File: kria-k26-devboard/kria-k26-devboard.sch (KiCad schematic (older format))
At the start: 1 part

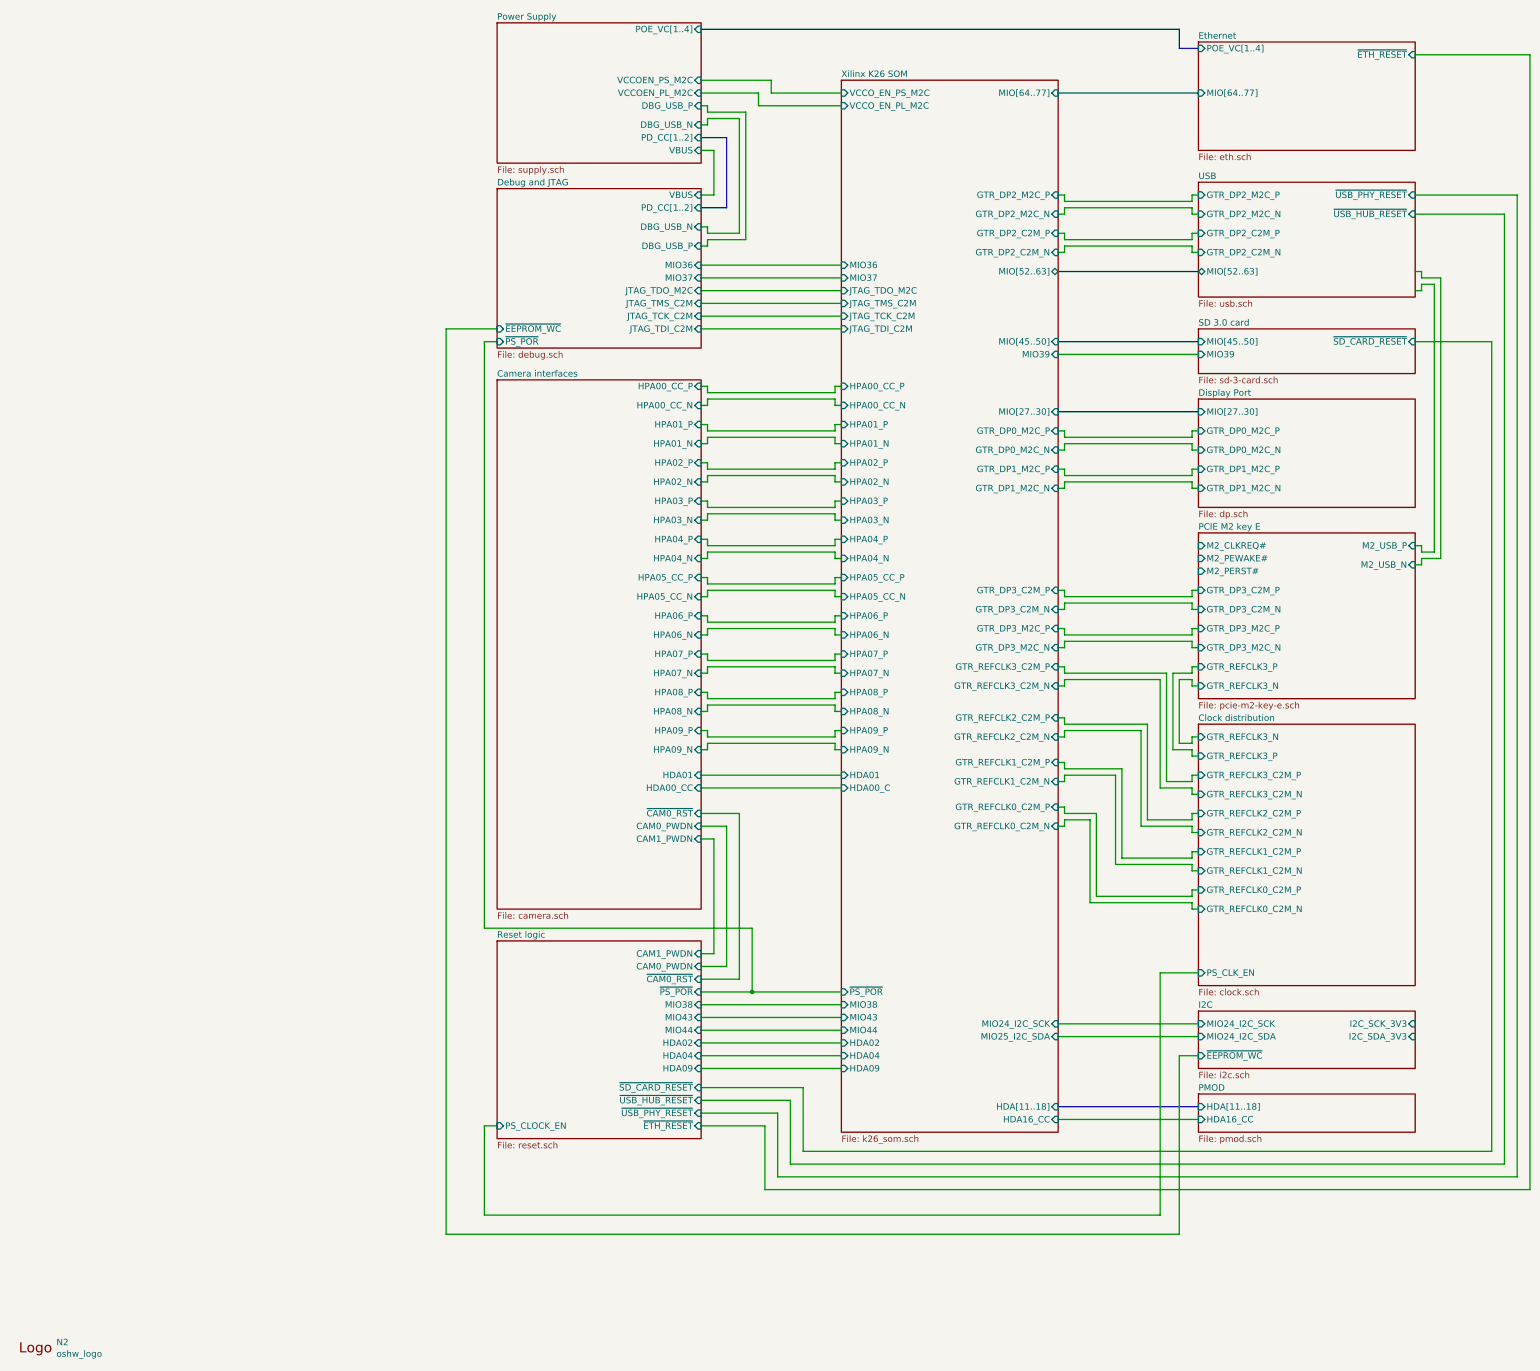
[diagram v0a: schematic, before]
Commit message: Added Led voltage indicator, fan circuit. Tidied up supply and SOM sheet
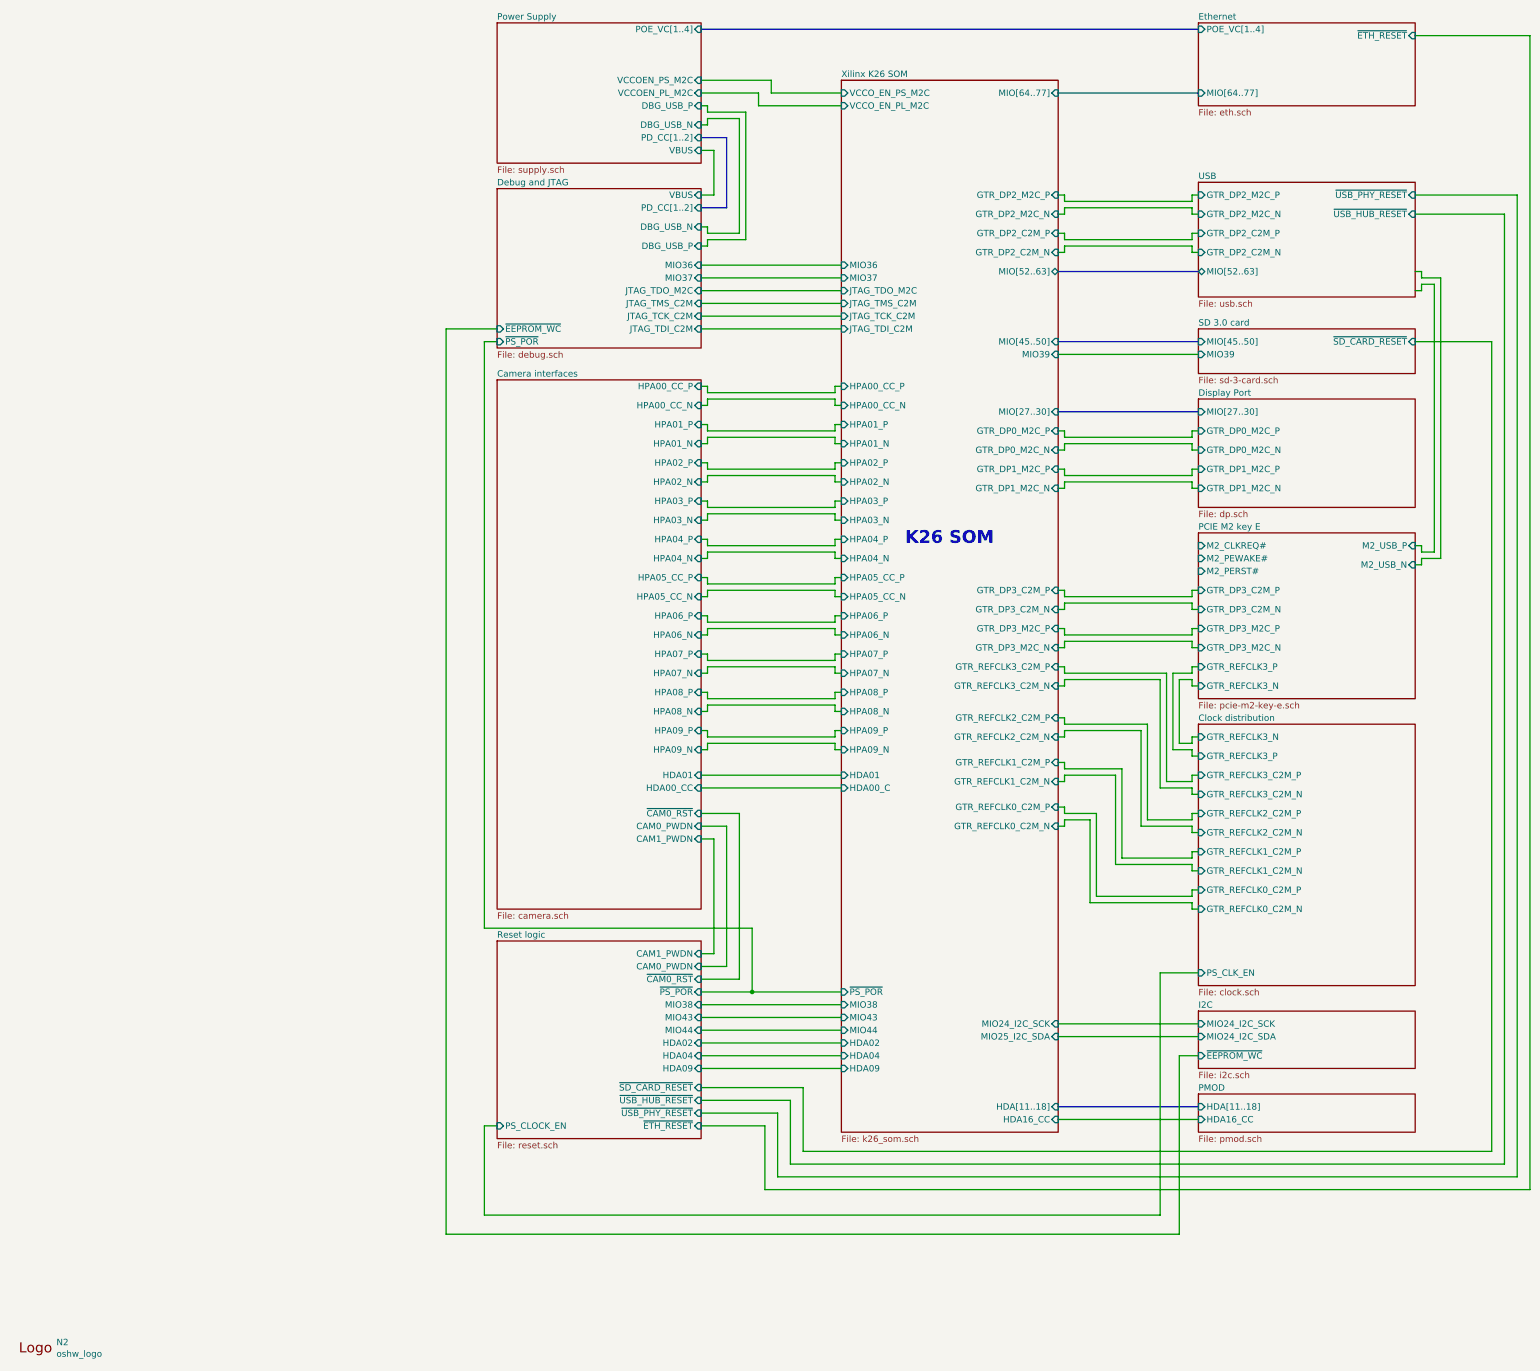
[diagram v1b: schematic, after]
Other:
- note added: "K26 SOM"
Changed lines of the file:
@@
 $EndSheet
-Wire Wire Line
-	12450 9800 12450 900
 Wire Wire Line
 	12150 3150 11550 3150
@@
 	12350 2000 12350 9700
 Wire Wire Line
-	12450 900  11550 900
+	12450 750  11550 750
 Wire Wire Line
 	5950 2250 6000 2250
@@
 F2 "MIO24_I2C_SCK" I L 9850 8500 50
 F3 "MIO24_I2C_SDA" I L 9850 8600 50
-F4 "I2C_SDA_3V3" I R 11550 8600 50
-F5 "I2C_SCK_3V3" I R 11550 8500 50
-F6 "~EEPROM_WC" I L 9850 8750 50
+F4 "~EEPROM_WC" I L 9850 8750 50
 $EndSheet
 Wire Wire Line
@@
 Wire Wire Line
 	6050 1650 5950 1650
-Wire Bus Line
-	5950 700  9700 700
-Wire Bus Line
-	9700 700  9700 850
-Wire Bus Line
-	9700 850  9850 850
 $Sheet
 S 9850 1900 1700 900
@@
 $EndSheet
 $Sheet
-S 9850 800  1700 850
+S 9850 650  1700 650
 U 63C3FA95
 F0 "Ethernet" 50
 F1 "eth.sch" 50
 F2 "MIO[64..77]" I L 9850 1200 50
-F3 "POE_VC[1..4]" I L 9850 850 50
-F4 "~ETH_RESET" I R 11550 900 50
+F3 "POE_VC[1..4]" I L 9850 700 50
+F4 "~ETH_RESET" I R 11550 750 50
 $EndSheet
 $Sheet
@@
 Wire Wire Line
 	9700 8750 9850 8750
+Wire Bus Line
+	5950 700  9850 700
+Wire Wire Line
+	12450 750  12450 9800
+Text Notes 7550 4750 0    100  ~ 20
+K26 SOM
 $EndSCHEMATC

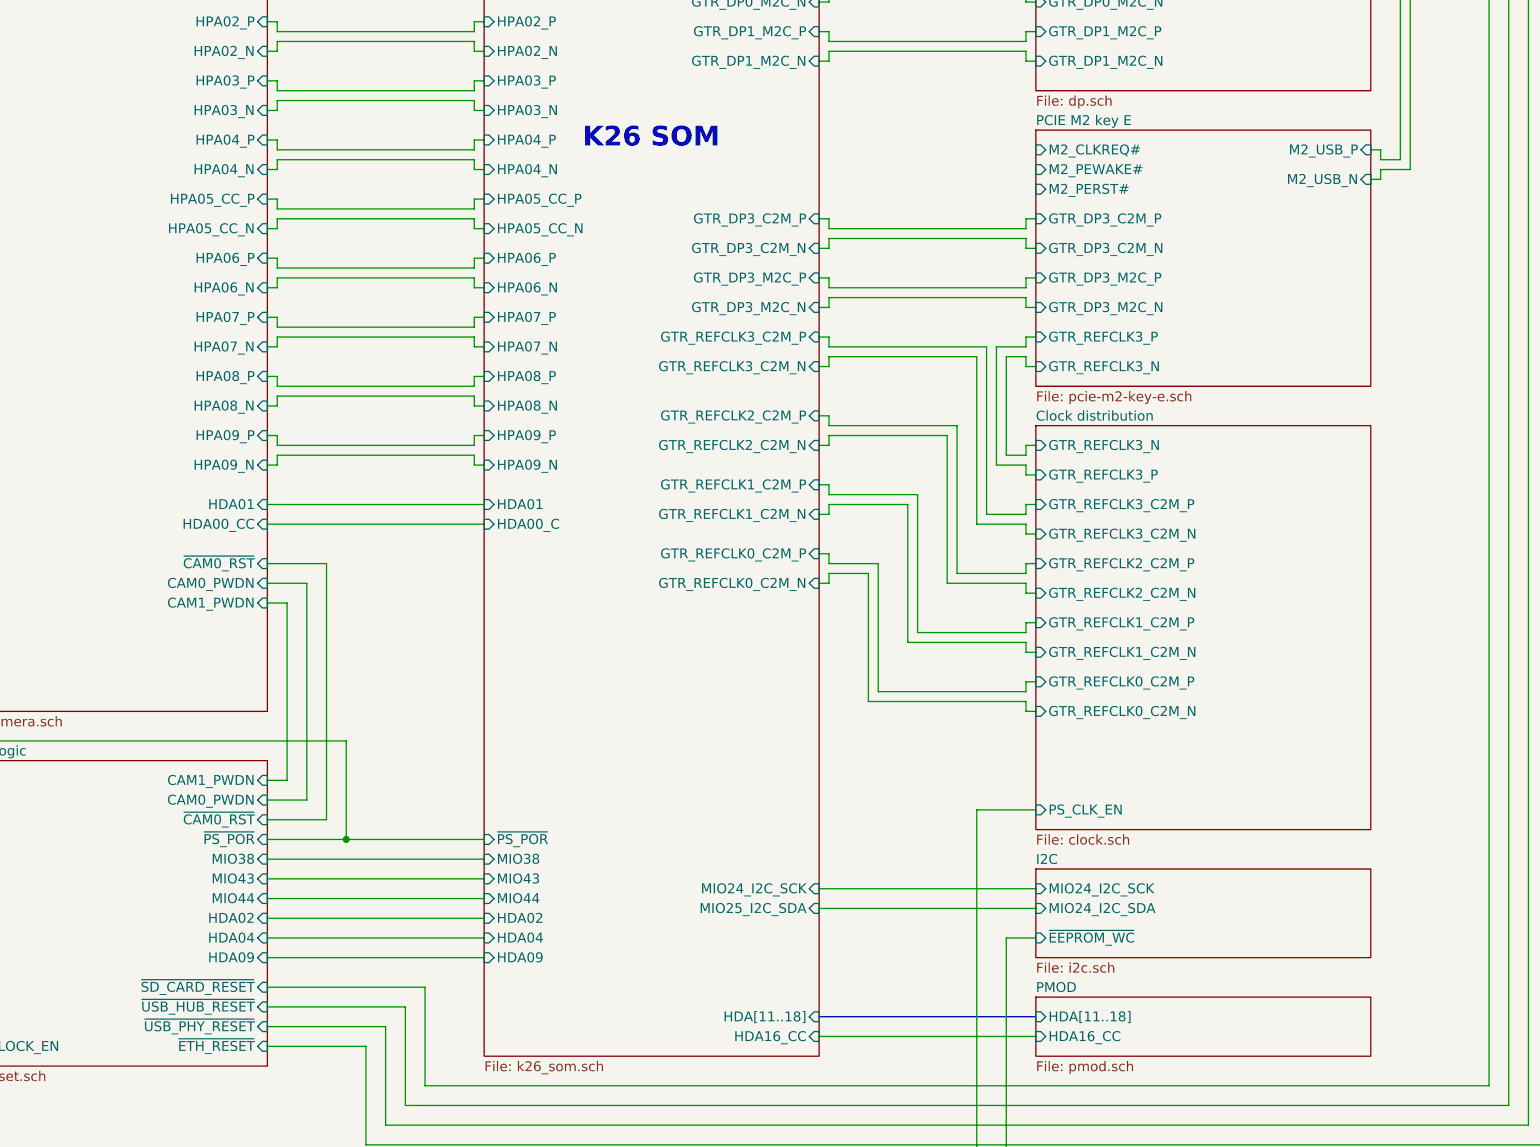
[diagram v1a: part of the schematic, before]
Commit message: fixed an issue with reset logic (Mixed PS and PL domain on OD buffer), extended the logic circuit to support M.2 PERST# (reset for PCIe WIFI), fixed the polarity of the camera control signal CAM_RST to comply with Antmicro standard, change CAM _SHDN to CAM_VSYNC, replaced the reset connector to fit additional signal M2_PERST
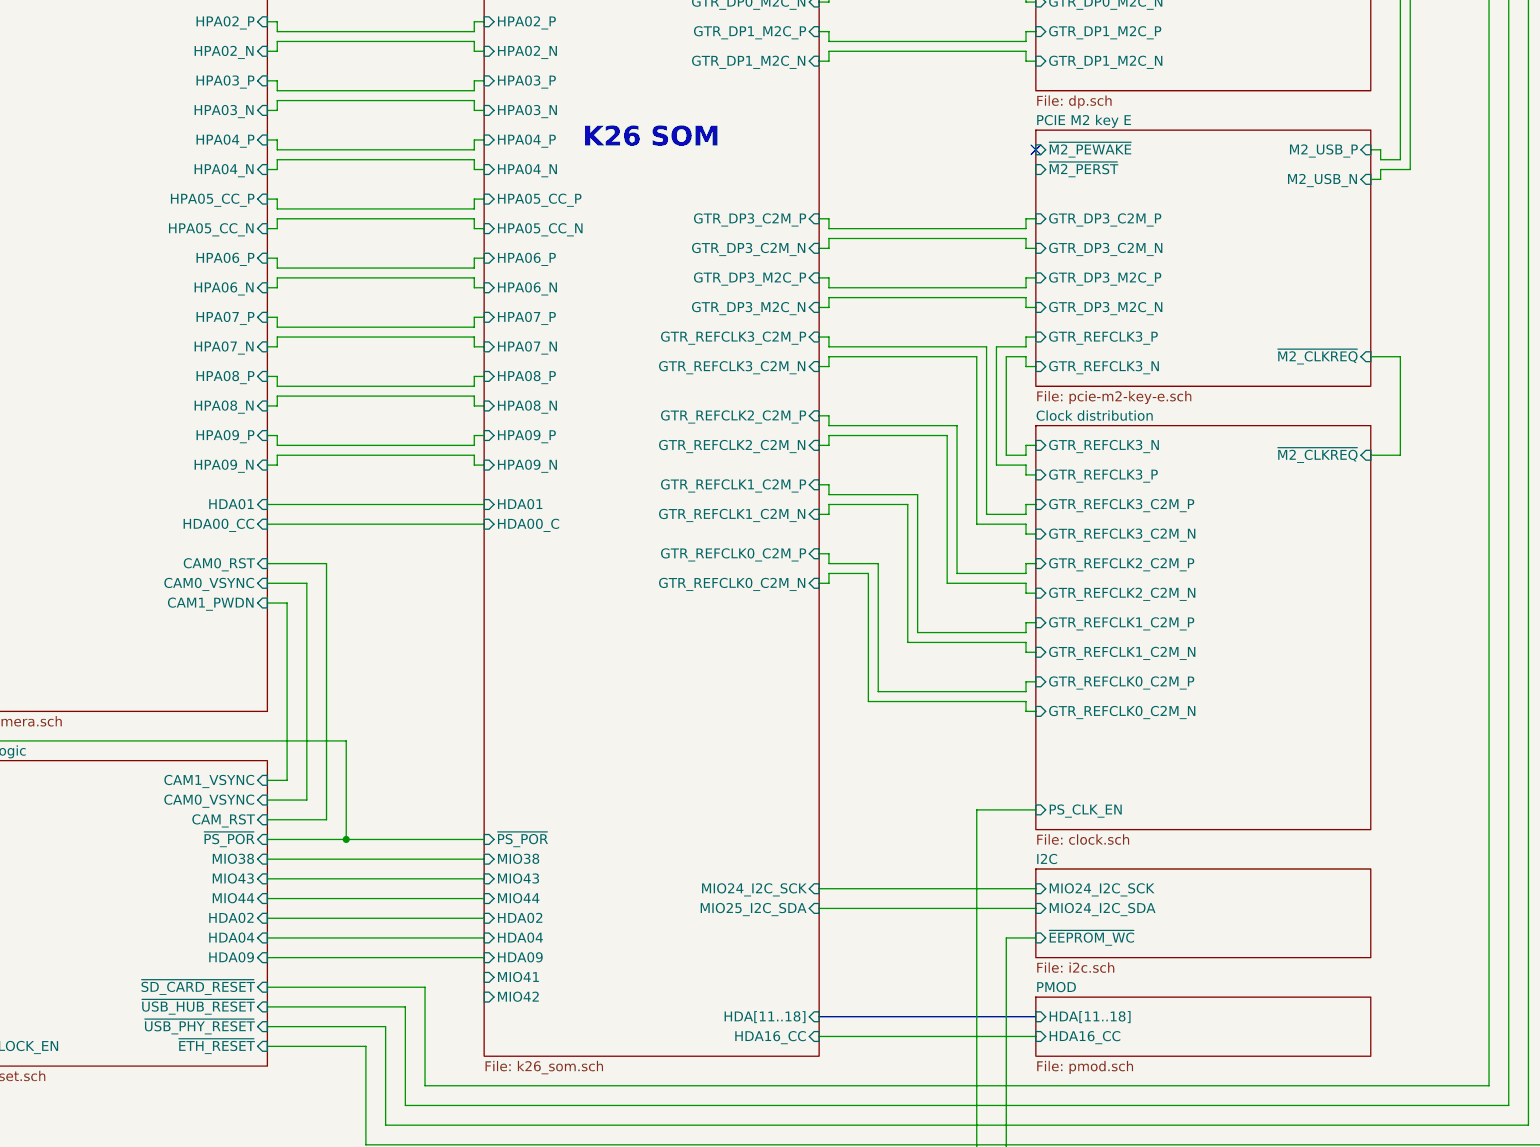
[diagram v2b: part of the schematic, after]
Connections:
- no-connect marks 0 -> 1
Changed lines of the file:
@@
 F6 "GTR_REFCLK3_P" I L 9850 5700 50
 F7 "GTR_REFCLK3_N" I L 9850 5850 50
-F8 "M2_CLKREQ#" I L 9850 4750 50
-F9 "M2_PEWAKE#" I L 9850 4850 50
-F10 "M2_PERST#" I L 9850 4950 50
-F11 "M2_USB_P" I R 11550 4750 50
-F12 "M2_USB_N" I R 11550 4900 50
+F8 "M2_USB_P" I R 11550 4750 50
+F9 "M2_USB_N" I R 11550 4900 50
+F10 "~M2_CLKREQ" I R 11550 5800 50
+F11 "~M2_PEWAKE" I L 9850 4750 50
+F12 "~M2_PERST" I L 9850 4850 50
 $EndSheet
 Wire Wire Line
@@
 F11 "GTR_REFCLK0_C2M_P" I L 9850 7450 50
 F12 "GTR_REFCLK0_C2M_N" I L 9850 7600 50
+F13 "~M2_CLKREQ" I R 11550 6300 50
 $EndSheet
 Wire Wire Line
@@
 F22 "HDA01" I R 5950 6550 50
 F23 "HDA00_CC" I R 5950 6650 50
-F24 "CAM0_PWDN" I R 5950 6950 50
-F25 "CAM1_PWDN" I R 5950 7050 50
-F26 "~CAM0_RST" I R 5950 6850 50
+F24 "CAM0_RST" I R 5950 6850 50
+F25 "CAM0_VSYNC" I R 5950 6950 50
+F26 "CAM1_PWDN" I R 5950 7050 50
 $EndSheet
 Wire Wire Line
@@
 Wire Wire Line
 	7050 8850 5950 8850
-$Sheet
-S 4350 7850 1600 1550
-U 65AAF1BF
-F0 "Reset logic" 50
-F1 "reset.sch" 50
-F2 "MIO43" I R 5950 8450 50
-F3 "MIO44" I R 5950 8550 50
-F4 "MIO38" I R 5950 8350 50
-F5 "CAM0_PWDN" I R 5950 8050 50
-F6 "CAM1_PWDN" I R 5950 7950 50
-F7 "HDA02" I R 5950 8650 50
-F8 "HDA04" I R 5950 8750 50
-F9 "HDA09" I R 5950 8850 50
-F10 "~PS_POR" I R 5950 8250 50
-F11 "~USB_PHY_RESET" I R 5950 9200 50
-F12 "~USB_HUB_RESET" I R 5950 9100 50
-F13 "~ETH_RESET" I R 5950 9300 50
-F14 "~CAM0_RST" I R 5950 8150 50
-F15 "~SD_CARD_RESET" I R 5950 9000 50
-F16 "PS_CLOCK_EN" I L 4350 9300 50
-$EndSheet
 Wire Wire Line
 	5950 9000 6750 9000
@@
 F66 "GTR_REFCLK0_C2M_P" I R 8750 6800 50
 F67 "GTR_REFCLK0_C2M_N" I R 8750 6950 50
+F68 "MIO41" I L 7050 8950 50
+F69 "MIO42" I L 7050 9050 50
 $EndSheet
 Wire Wire Line
@@
 Text Notes 7550 4750 0    100  ~ 20
 K26 SOM
+Wire Wire Line
+	11550 5800 11700 5800
+Wire Wire Line
+	11700 5800 11700 6300
+Wire Wire Line
+	11700 6300 11550 6300
+NoConn ~ 9850 4750
+$Sheet
+S 4350 7850 1600 1550
+U 65AAF1BF
+F0 "Reset logic" 50
+F1 "reset.sch" 50
+F2 "MIO43" I R 5950 8450 50
+F3 "MIO44" I R 5950 8550 50
+F4 "MIO38" I R 5950 8350 50
+F5 "HDA02" I R 5950 8650 50
+F6 "HDA04" I R 5950 8750 50
+F7 "HDA09" I R 5950 8850 50
+F8 "~PS_POR" I R 5950 8250 50
+F9 "~USB_PHY_RESET" I R 5950 9200 50
+F10 "~USB_HUB_RESET" I R 5950 9100 50
+F11 "~ETH_RESET" I R 5950 9300 50
+F12 "~SD_CARD_RESET" I R 5950 9000 50
+F13 "PS_CLOCK_EN" I L 4350 9300 50
+F14 "CAM_RST" I R 5950 8150 50
+F15 "CAM0_VSYNC" I R 5950 8050 50
+F16 "CAM1_VSYNC" I R 5950 7950 50
+$EndSheet
 $EndSCHEMATC
